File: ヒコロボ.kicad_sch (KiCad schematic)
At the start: 5 parts, among them U1 R3106GF, U2 4053, U3 4053, U5 R3106FG_IF

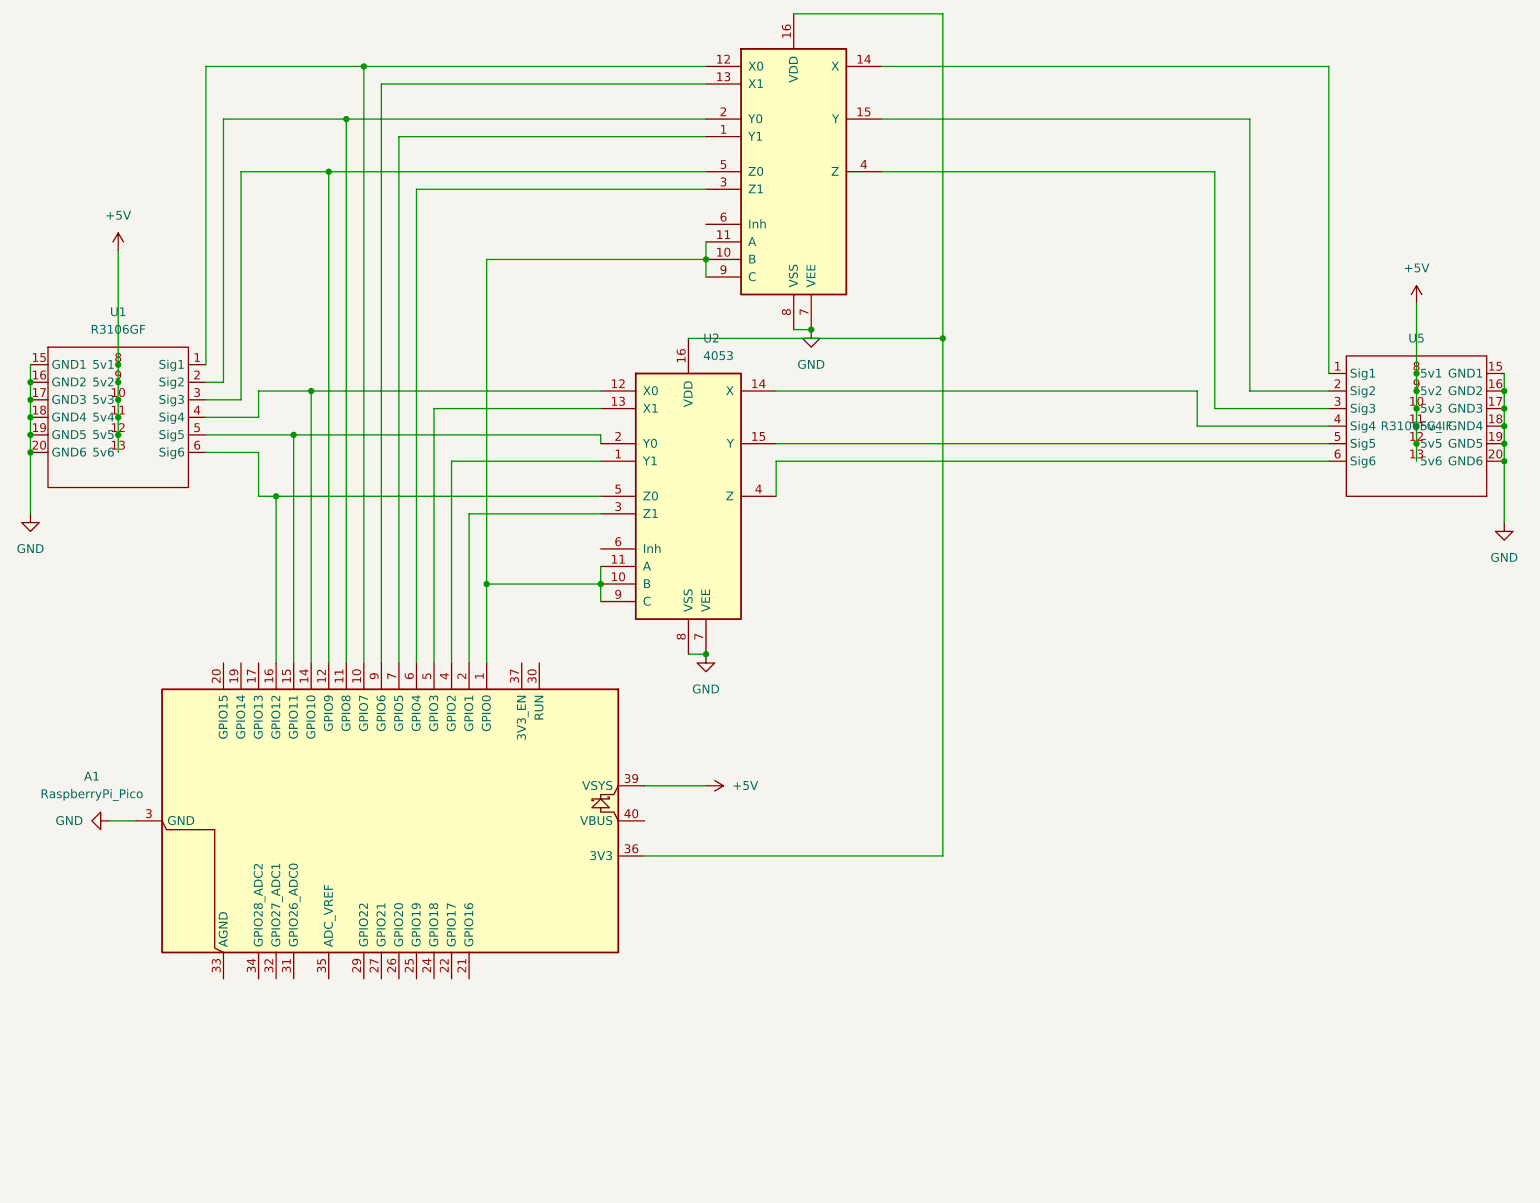
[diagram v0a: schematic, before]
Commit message: update sensor IF
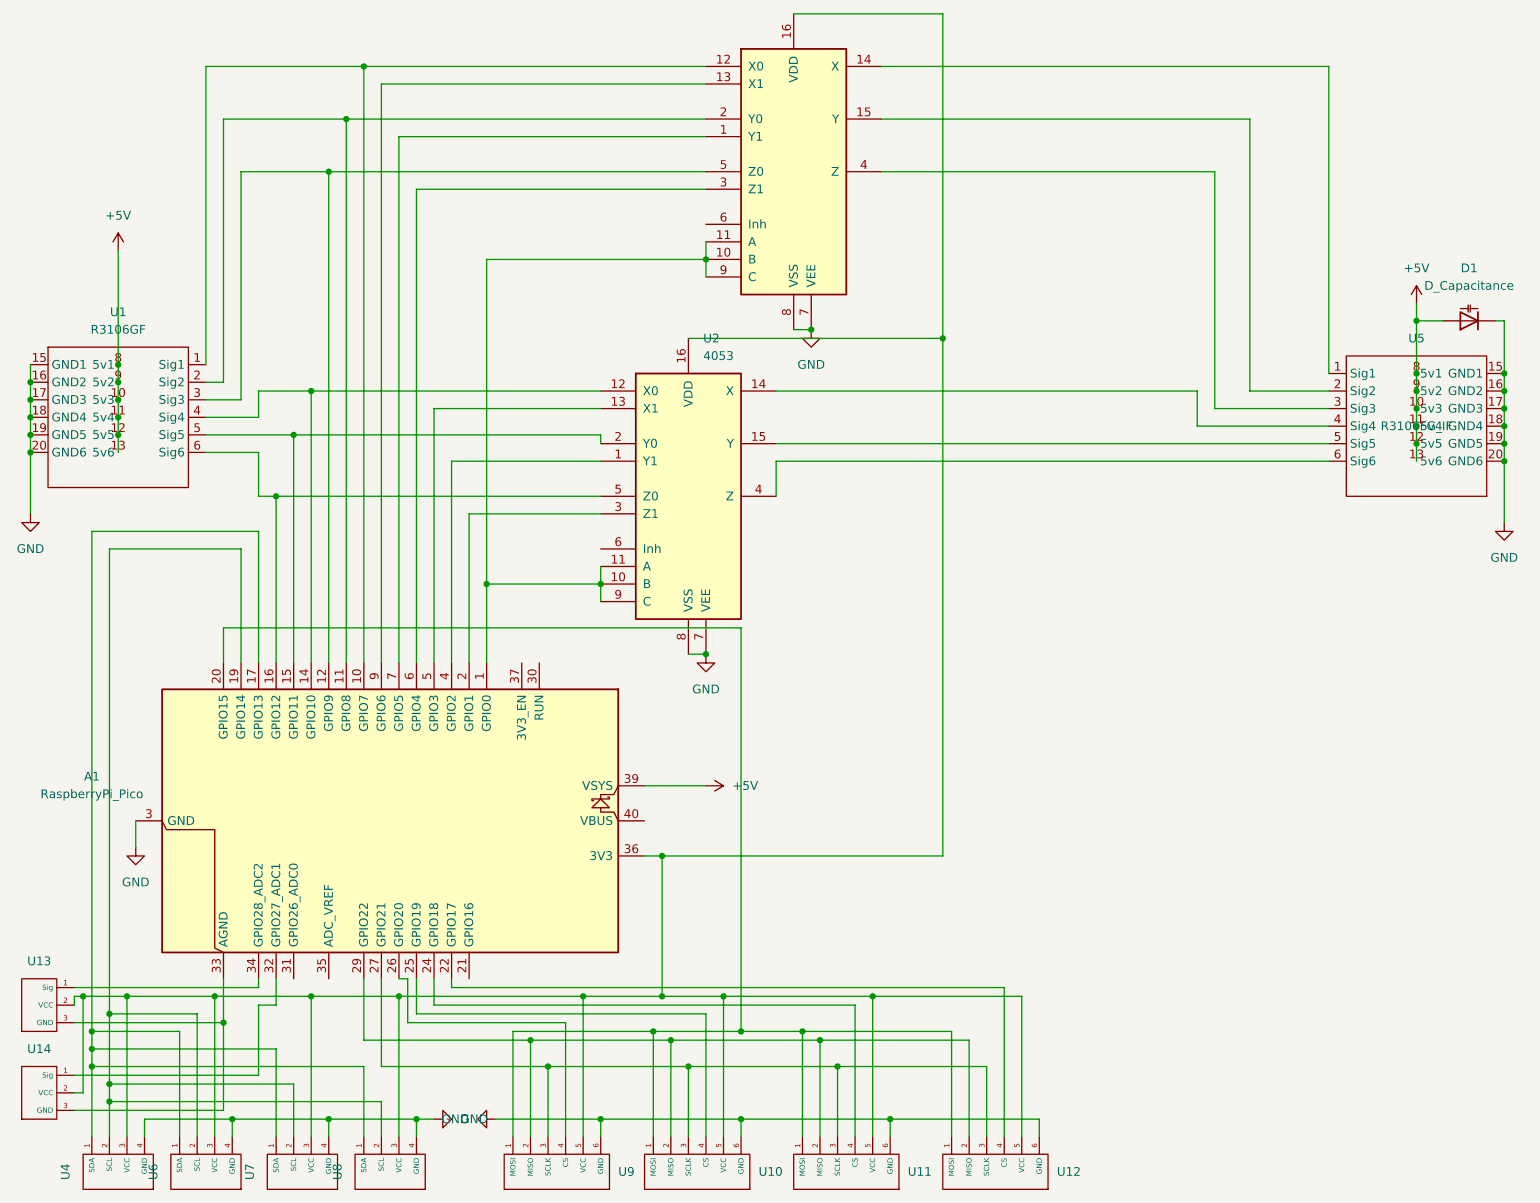
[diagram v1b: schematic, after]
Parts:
- added D1: D_Capacitance, Capacitor_SMD:CP_Elec_8x10.5, symbol Device:D_Capacitance
- added U10, U11, U12, U9: (no value), Library:Sensor_SPI_IF, symbol My_Library:Sensor_SPI_IF
- added U13, U14: (no value), Library:Sensor_Analog_IF, symbol My_Library:Sensor_Analog_IF
- added U4, U6, U7, U8: (no value), Library:Sensor_I2C_IF, symbol My_Library:Sensor_IF
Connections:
- net +5V: now also D1.2 (A)
- net GND: now also D1.1 (K), U10.6 (GND), U11.6 (GND), U12.6 (GND), U4.4 (GND), U6.4 (GND), U7.4 (GND), U8.4 (GND), U9.6 (GND)
- net at A1.36 (3V3), U2.16 (VDD), U3.16 (VDD): now also U10.5 (VCC), U11.5 (VCC), U12.5 (VCC), U13.2 (VCC), U14.2 (VCC), U4.3 (VCC), U6.3 (VCC), U7.3 (VCC), U8.3 (VCC), U9.5 (VCC)
- net at A1.17 (GPIO13): now also U4.1 (SDA), U6.1 (SDA), U7.1 (SDA), U8.1 (SDA)
- net at A1.19 (GPIO14): now also U4.2 (SCL), U6.2 (SCL), U7.2 (SCL), U8.2 (SCL)
- net at A1.20 (GPIO15): now also U10.1 (MOSI), U11.1 (MOSI), U12.1 (MOSI), U9.1 (MOSI)
- net at A1.22 (GPIO17): now also U12.4 (CS)
- net at A1.24 (GPIO18): now also U11.4 (CS)
- net at A1.25 (GPIO19): now also U10.4 (CS)
- net at A1.26 (GPIO20): now also U9.4 (CS)
- net at A1.27 (GPIO21): now also U10.3 (SCLK), U11.3 (SCLK), U12.3 (SCLK), U9.3 (SCLK)
- net at A1.29 (GPIO22): now also U10.2 (MISO), U11.2 (MISO), U12.2 (MISO), U9.2 (MISO)
- net at A1.32 (GPIO27_ADC1): now also U14.1 (Sig)
- net at A1.33 (AGND): now also U13.3 (GND), U14.3 (GND)
- net at A1.34 (GPIO28_ADC2): now also U13.1 (Sig)
